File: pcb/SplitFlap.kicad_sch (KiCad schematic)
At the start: 22 parts, among them J1 A1_3, U1 PCF8575DBR, U2 ULN2003, U4 AP2112K-3.3

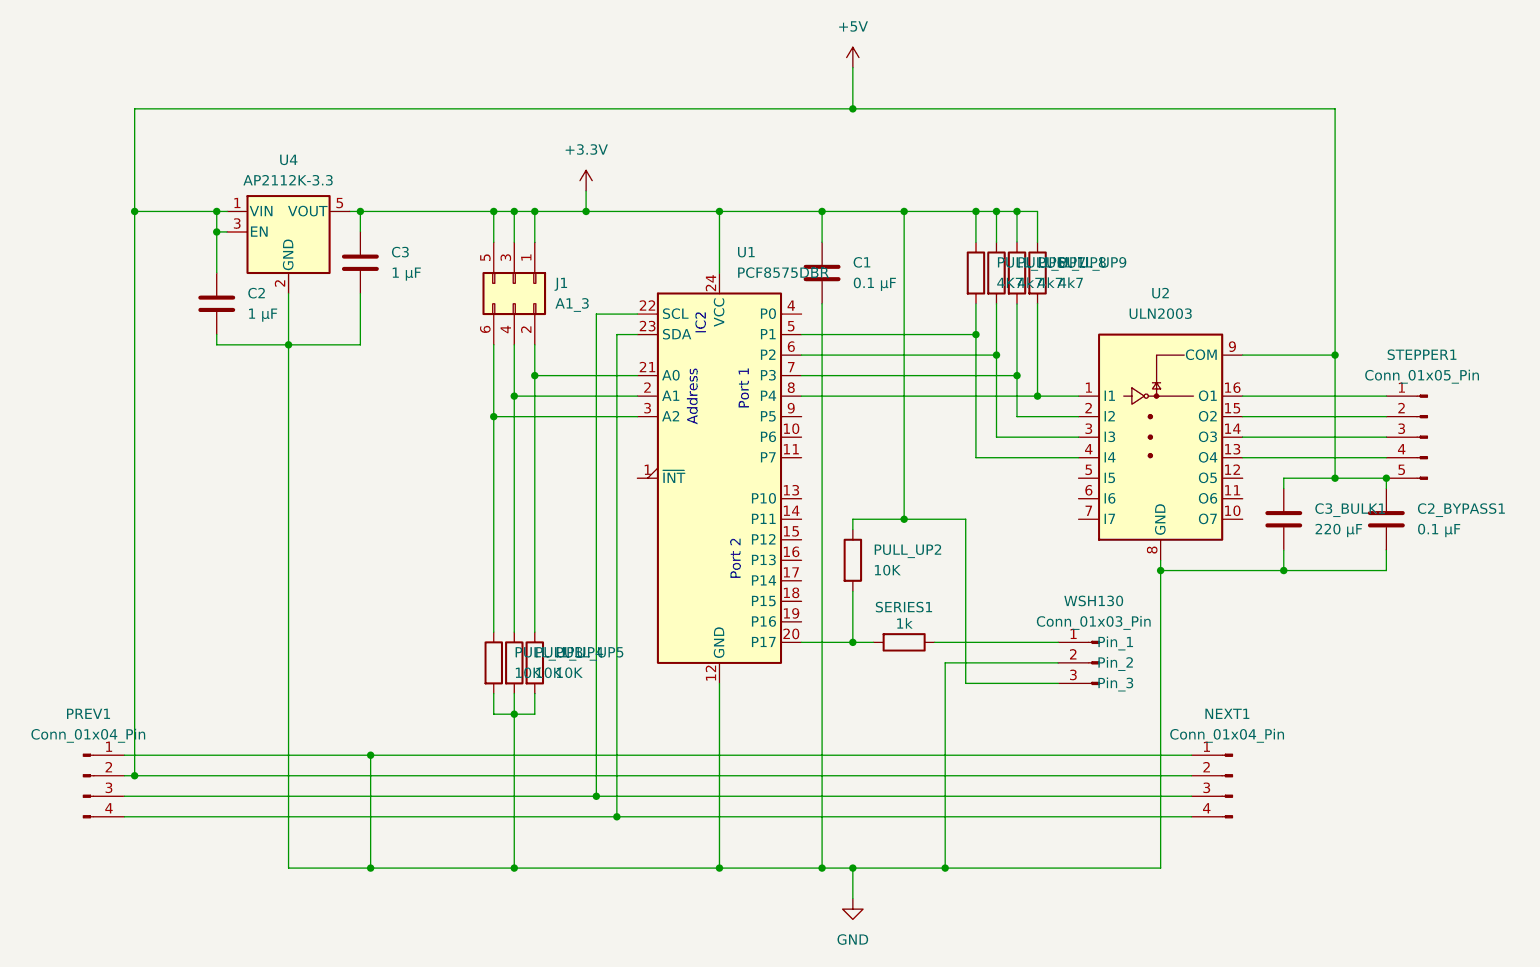
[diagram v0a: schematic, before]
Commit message: Eliminate 3.3v line from PCB
Based on the findings by FoxManJ the 3.3v line is not required if we
use a 4.7k Ohm pull-up to 5v for the SCL and SDA lines coming from the
ESP32.

By using this pull-up to 5V we eliminate the need for the PCF8575 to
run at 3.3v to understand the signals from the ESP32, which was the
reason I originally implemented the 3.3v line on each board.
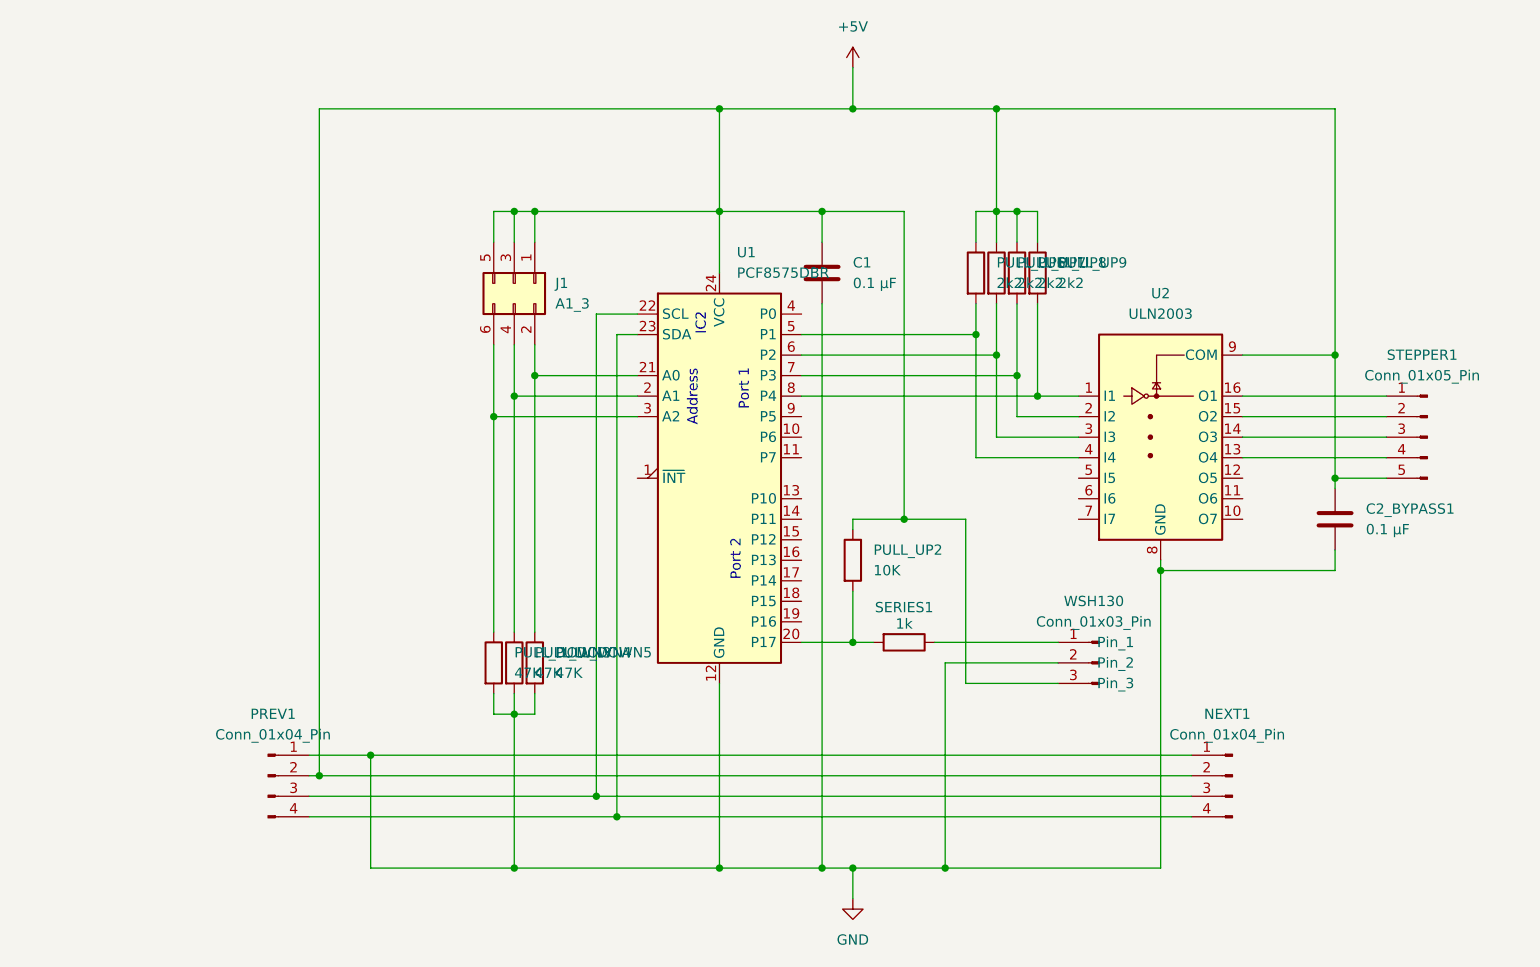
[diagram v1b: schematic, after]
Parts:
- removed C2, C3: 1 µF, Capacitor_SMD:C_0603_1608Metric, symbol Device:C
- removed C3_BULK1: 220 µF, Capacitor_SMD:C_Elec_6.3x7.7, symbol Device:C
- removed U4: AP2112K-3.3, Package_TO_SOT_SMD:SOT-23-5, symbol Regulator_Linear:AP2112K-3.3
- PULL_DOWN3: renamed from PULL_UP3; value 10K -> 47K
- PULL_DOWN4: renamed from PULL_UP4; value 10K -> 47K
- PULL_DOWN5: renamed from PULL_UP5; value 10K -> 47K
- PULL_UP6: value 4K7 -> 2k2
- PULL_UP7, PULL_UP8, PULL_UP9: value 4k7 -> 2k2
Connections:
- net +3.3V is gone; now on net +5V: C1.1, J1.1 (Pin_1), J1.3 (Pin_3), J1.5 (Pin_5), PULL_UP2.1, PULL_UP6.1, PULL_UP7.1, PULL_UP8.1, PULL_UP9.1, U1.24 (VCC), WSH130.3 (Pin_3)
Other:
- moved on the sheet: C2_BYPASS1, PREV1

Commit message: Use pinsocket and headers for board to board connector
Eliminates the JST cables between boards.
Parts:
- J1: MPN (none) -> C7501594
- NEXT1: footprint Connector_JST:JST_PH_B4B-PH-K_1x04_P2.00mm_Vertical -> Connector_PinSocket_2.54mm:PinSocket_1x04_P2.54mm_Horizontal; MPN C2321 -> C6297769
- PREV1: footprint Connector_JST:JST_PH_B4B-PH-K_1x04_P2.00mm_Vertical -> Connector_PinHeader_2.54mm:PinHeader_1x04_P2.54mm_Horizontal; MPN C2321 -> C22438278
- PULL_DOWN3, PULL_DOWN4, PULL_DOWN5: MPN C73809 -> C25600
- PULL_UP6, PULL_UP7, PULL_UP8, PULL_UP9: MPN C23162 -> C4190
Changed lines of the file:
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@@
 			)
 		)
-		(property "MPN" "C23162"
+		(property "MPN" "C4190"
 			(at 165.1 68.58 0)
 			(effects
@@
 			)
 		)
-		(property "MPN" "C73809"
+		(property "MPN" "C25600"
 			(at 97.79 116.84 0)
 			(effects
@@
 			)
 		)
-		(property "MPN" "C73809"
+		(property "MPN" "C25600"
 			(at 100.33 116.84 0)
 			(effects
@@
 			)
 		)
-		(property "MPN" "C23162"
+		(property "MPN" "C4190"
 			(at 160.02 68.58 0)
 			(effects
@@
 			)
 		)
-		(property "Footprint" "Connector_JST:JST_PH_B4B-PH-K_1x04_P2.00mm_Vertical"
+		(property "Footprint" "Connector_PinSocket_2.54mm:PinSocket_1x04_P2.54mm_Horizontal"
 			(at 189.23 130.81 0)
 			(effects
@@
 			)
 		)
-		(property "MPN" "C2321"
+		(property "MPN" "C6297769"
 			(at 189.23 130.81 0)
 			(effects
@@
 			)
 		)
-		(property "MPN" "C23162"
+		(property "MPN" "C4190"
 			(at 157.48 68.58 0)
 			(effects
@@
 			)
 		)
-		(property "MPN" "C73809"
+		(property "MPN" "C25600"
 			(at 102.87 116.84 0)
 			(effects
@@
 			)
 		)
+		(property "MPN" "C7501594"
+			(at 100.33 69.85 90)
+			(effects
+				(font
+					(size 1.27 1.27)
+				)
+				(hide yes)
+			)
+		)
 		(pin "1"
 		)
@@
 			)
 		)
-		(property "Footprint" "Connector_JST:JST_PH_B4B-PH-K_1x04_P2.00mm_Vertical"
+		(property "Footprint" "Connector_PinHeader_2.54mm:PinHeader_1x04_P2.54mm_Horizontal"
 			(at 69.85 130.81 0)
 			(effects
@@
 			)
 		)
-		(property "MPN" "C2321"
+		(property "MPN" "C22438278"
 			(at 69.85 130.81 0)
 			(effects
@@
 			)
 		)
-		(property "MPN" "C23162"
+		(property "MPN" "C4190"
 			(at 162.56 68.58 0)
 			(effects

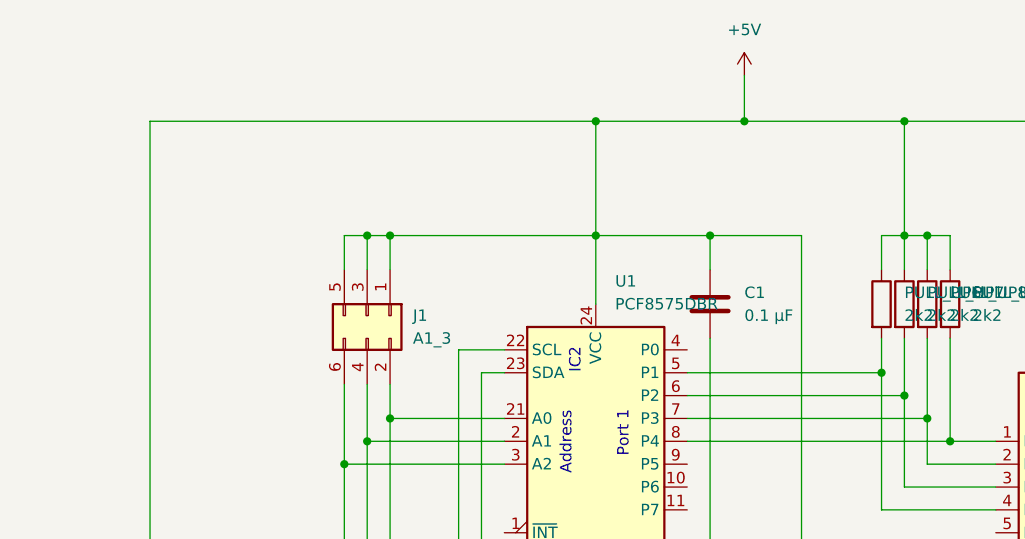
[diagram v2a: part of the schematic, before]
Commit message: Add optional data lines pull-up
Required as the ESP32 by default does not pull up the data lines to
5v.  Should only be activated once per circuit (display).
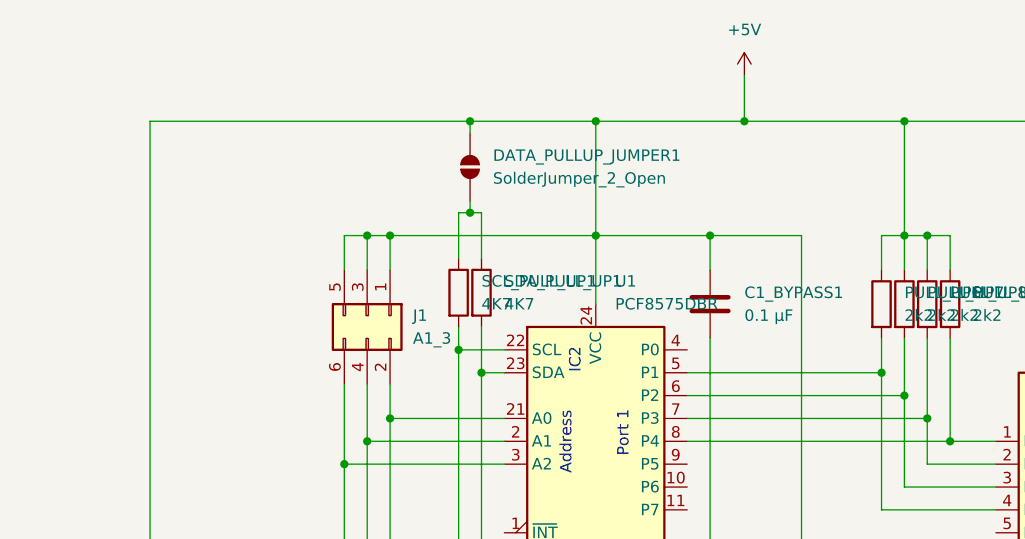
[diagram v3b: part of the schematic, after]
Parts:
- added DATA_PULLUP_JUMPER1: SolderJumper_2_Open, Jumper:SolderJumper-2_P1.3mm_Open_RoundedPad1.0x1.5mm, symbol Jumper:SolderJumper_2_Open
- added SCL_PULL_UP1, SDA_PULL_UP1: 4K7, Resistor_SMD:R_0603_1608Metric, symbol Device:R
- C1_BYPASS1: renamed from C1; MPN C6955083 -> C1525
- C2_BYPASS1: MPN C6955083 -> C1525
- NEXT1: MPN C6297769 -> C2897386
- PREV1: MPN C22438278 -> C91552
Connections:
- net +5V: now also DATA_PULLUP_JUMPER1.1 (A)
- net at NEXT1.3 (Pin_3), PREV1.3 (Pin_3), U1.22 (SCL): now also SCL_PULL_UP1.2
- net at NEXT1.4 (Pin_4), PREV1.4 (Pin_4), U1.23 (SDA): now also SDA_PULL_UP1.2
- new net: DATA_PULLUP_JUMPER1.2 (B), SCL_PULL_UP1.1, SDA_PULL_UP1.1

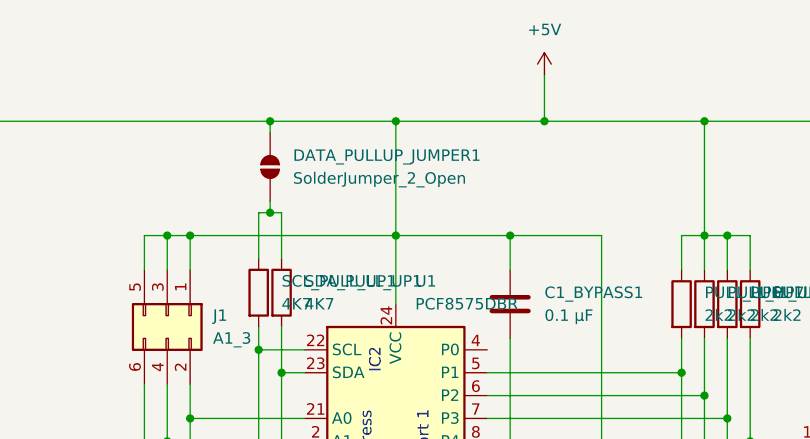
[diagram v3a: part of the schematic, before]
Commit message: Rename pull-up jumper
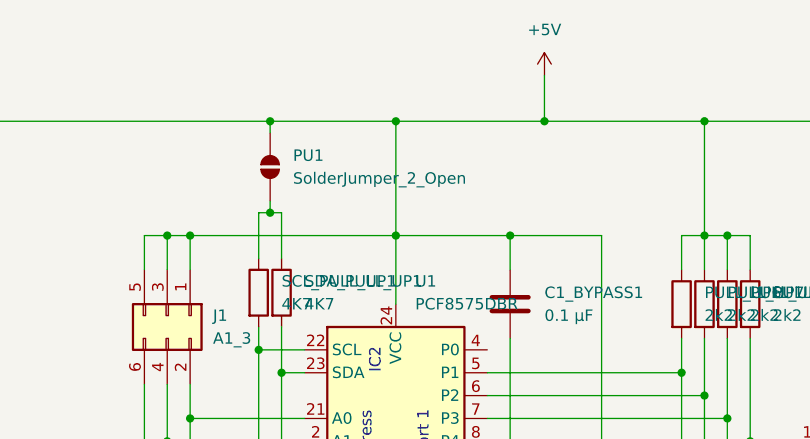
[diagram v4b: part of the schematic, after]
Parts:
- renumbered DATA_PULLUP_JUMPER1 to PU1
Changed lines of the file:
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@@
 		(dnp no)
 		(fields_autoplaced yes)
-		(property "Reference" "DATA_PULLUP_JUMPER1"
+		(property "Reference" "PU1"
 			(at 114.3 52.0699 90)
 			(effects
@@
 			(project ""
 				(path "/a27c2069-9cb4-4119-a6b4-dc99fc554c69"
-					(reference "DATA_PULLUP_JUMPER1")
+					(reference "PU1")
 					(unit 1)
 				)

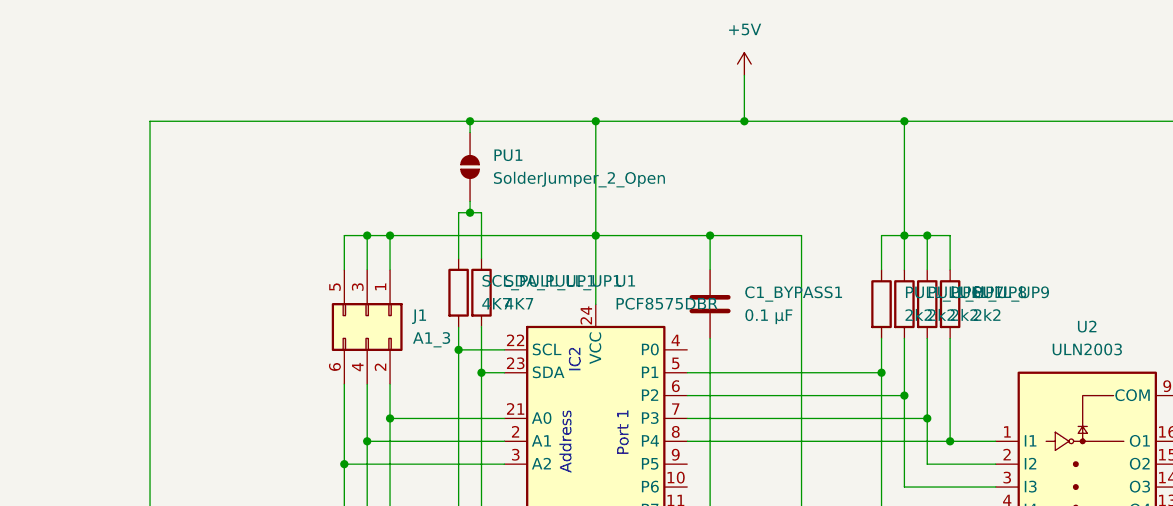
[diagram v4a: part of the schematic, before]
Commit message: Fix floating pull-ups
The optional pull-ups added in v4 added an unintentional floating node
that would tie SCL and SDA together whenever the pull-up pad was
unsoldered.  Causing the I2C bus to fail (surprisingly only after
connecting 3 modules).
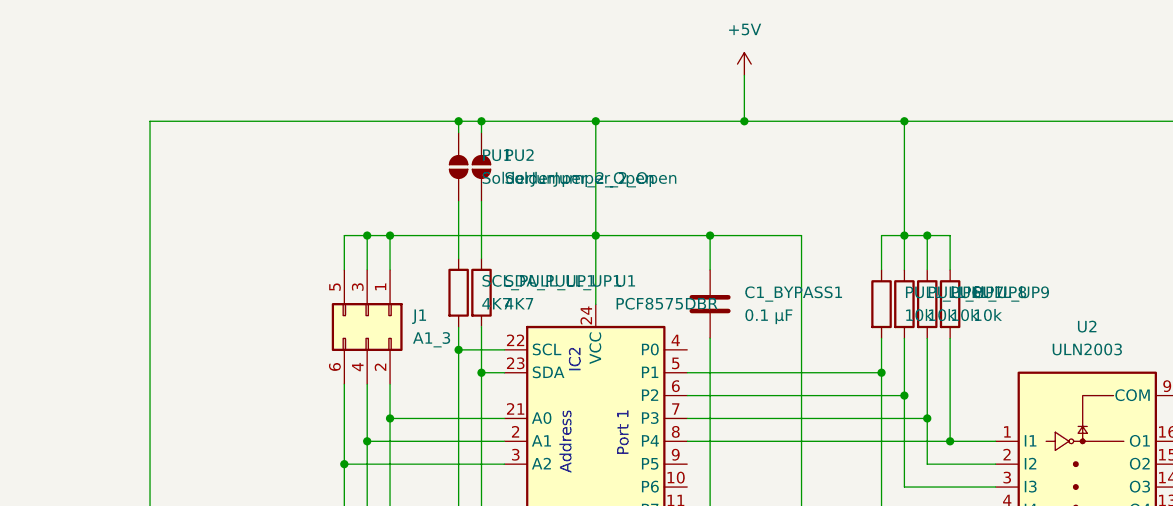
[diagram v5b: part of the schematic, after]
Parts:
- added PU2: SolderJumper_2_Open, Jumper:SolderJumper-2_P1.3mm_Open_RoundedPad1.0x1.5mm, symbol Jumper:SolderJumper_2_Open
- PULL_UP6, PULL_UP7, PULL_UP8, PULL_UP9: value 2k2 -> 10k; MPN C4190 -> C73809
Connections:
- net +5V: now also PU2.1 (A)
- net at PU1.2 (B), SCL_PULL_UP1.1: no longer SDA_PULL_UP1.1
- new net: PU2.2 (B), SDA_PULL_UP1.1
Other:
- moved on the sheet: PU1
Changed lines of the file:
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@@
+	)
+	(junction
+		(at 113.03 48.26)
+		(diameter 0)
+		(color 0 0 0 0)
 	)
 	(junction
@@
 	)
 	(junction
-		(at 111.76 48.26)
-		(diameter 0)
-		(color 0 0 0 0)
-	)
-	(junction
 		(at 160.02 60.96)
 		(diameter 0)
@@
 	)
 	(junction
+		(at 110.49 48.26)
+		(diameter 0)
+		(color 0 0 0 0)
+	)
+	(junction
 		(at 100.33 83.82)
 		(diameter 0)
@@
 	)
 	(junction
-		(at 111.76 58.42)
-		(diameter 0)
-		(color 0 0 0 0)
-	)
-	(junction
 		(at 138.43 60.96)
 		(diameter 0)
@@
 	(wire
 		(pts
-			(xy 76.2 48.26) (xy 111.76 48.26)
+			(xy 76.2 48.26) (xy 110.49 48.26)
 		)
 		(stroke
@@
 	(wire
 		(pts
-			(xy 111.76 58.42) (xy 113.03 58.42)
-		)
-		(stroke
-			(width 0)
-			(type default)
-		)
-	)
-	(wire
-		(pts
 			(xy 162.56 60.96) (xy 165.1 60.96)
 		)
@@
 	(wire
 		(pts
-			(xy 110.49 63.5) (xy 110.49 58.42)
+			(xy 110.49 57.15) (xy 110.49 63.5)
 		)
 		(stroke
@@
 	(wire
 		(pts
+			(xy 113.03 48.26) (xy 125.73 48.26)
+		)
+		(stroke
+			(width 0)
+			(type default)
+		)
+	)
+	(wire
+		(pts
 			(xy 100.33 60.96) (xy 100.33 64.77)
 		)
@@
 	(wire
 		(pts
-			(xy 111.76 48.26) (xy 125.73 48.26)
-		)
-		(stroke
-			(width 0)
-			(type default)
-		)
-	)
-	(wire
-		(pts
 			(xy 142.24 107.95) (xy 142.24 114.3)
 		)
@@
 	(wire
 		(pts
-			(xy 111.76 57.15) (xy 111.76 58.42)
-		)
-		(stroke
-			(width 0)
-			(type default)
-		)
-	)
-	(wire
-		(pts
 			(xy 160.02 72.39) (xy 160.02 78.74)
 		)
@@
 	(wire
 		(pts
+			(xy 110.49 48.26) (xy 113.03 48.26)
+		)
+		(stroke
+			(width 0)
+			(type default)
+		)
+	)
+	(wire
+		(pts
 			(xy 110.49 133.35) (xy 184.15 133.35)
 		)
@@
 	(wire
 		(pts
-			(xy 113.03 58.42) (xy 113.03 63.5)
+			(xy 113.03 57.15) (xy 113.03 63.5)
 		)
 		(stroke
@@
 	(wire
 		(pts
+			(xy 113.03 48.26) (xy 113.03 49.53)
+		)
+		(stroke
+			(width 0)
+			(type default)
+		)
+	)
+	(wire
+		(pts
 			(xy 113.03 71.12) (xy 113.03 76.2)
 		)
@@
 	(wire
 		(pts
-			(xy 110.49 58.42) (xy 111.76 58.42)
-		)
-		(stroke
-			(width 0)
-			(type default)
-		)
-	)
-	(wire
-		(pts
 			(xy 115.57 83.82) (xy 100.33 83.82)
 		)
@@
 	(wire
 		(pts
-			(xy 111.76 48.26) (xy 111.76 49.53)
+			(xy 110.49 48.26) (xy 110.49 49.53)
 		)
 		(stroke
@@
 			)
 		)
-		(property "Value" "2k2"
+		(property "Value" "10k"
 			(at 167.64 69.8499 0)
 			(effects
@@
 			)
 		)
-		(property "MPN" "C4190"
+		(property "MPN" "C73809"
 			(at 165.1 68.58 0)
 			(effects
@@
 	(symbol
 		(lib_id "Jumper:SolderJumper_2_Open")
-		(at 111.76 53.34 270)
+		(at 110.49 53.34 270)
 		(unit 1)
 		(exclude_from_sim no)
@@
 		(fields_autoplaced yes)
 		(property "Reference" "PU1"
-			(at 114.3 52.0699 90)
+			(at 113.03 52.0699 90)
 			(effects
 				(font
@@
 		)
 		(property "Value" "SolderJumper_2_Open"
-			(at 114.3 54.6099 90)
+			(at 113.03 54.6099 90)
 			(effects
 				(font
@@
 		)
 		(property "Footprint" "Jumper:SolderJumper-2_P1.3mm_Open_RoundedPad1.0x1.5mm"
-			(at 111.76 53.34 0)
+			(at 110.49 53.34 0)
 			(effects
 				(font
@@
 		)
 		(property "Datasheet" "~"
-			(at 111.76 53.34 0)
+			(at 110.49 53.34 0)
 			(effects
 				(font
@@
 		)
 		(property "Description" "Solder Jumper, 2-pole, open"
-			(at 111.76 53.34 0)
+			(at 110.49 53.34 0)
 			(effects
 				(font
@@
 			)
 		)
-		(property "Value" "2k2"
+		(property "Value" "10k"
 			(at 162.56 69.8499 0)
 			(effects
@@
 			)
 		)
-		(property "MPN" "C4190"
+		(property "MPN" "C73809"
 			(at 160.02 68.58 0)
 			(effects
@@
 			)
 		)
-		(property "Value" "2k2"
+		(property "Value" "10k"
 			(at 160.02 69.8499 0)
 			(effects
@@
 			)
 		)
-		(property "MPN" "C4190"
+		(property "MPN" "C73809"
 			(at 157.48 68.58 0)
 			(effects
@@
 	)
 	(symbol
+		(lib_id "Jumper:SolderJumper_2_Open")
+		(at 113.03 53.34 270)
+		(unit 1)
+		(exclude_from_sim no)
+		(in_bom no)
+		(on_board yes)
+		(dnp no)
+		(fields_autoplaced yes)
+		(property "Reference" "PU2"
+			(at 115.57 52.0699 90)
+			(effects
+				(font
+					(size 1.27 1.27)
+				)
+				(justify left)
+			)
+		)
+		(property "Value" "SolderJumper_2_Open"
+			(at 115.57 54.6099 90)
+			(effects
+				(font
+					(size 1.27 1.27)
+				)
+				(justify left)
+			)
+		)
+		(property "Footprint" "Jumper:SolderJumper-2_P1.3mm_Open_RoundedPad1.0x1.5mm"
+			(at 113.03 53.34 0)
+			(effects
+				(font
+					(size 1.27 1.27)
+				)
+				(hide yes)
+			)
+		)
+		(property "Datasheet" "~"
+			(at 113.03 53.34 0)
+			(effects
+				(font
+					(size 1.27 1.27)
+				)
+				(hide yes)
+			)
+		)
+		(property "Description" "Solder Jumper, 2-pole, open"
+			(at 113.03 53.34 0)
+			(effects
+				(font
+					(size 1.27 1.27)
+				)
+				(hide yes)
+			)
+		)
+		(pin "2"
+		)
+		(pin "1"
+		)
+		(instances
+			(project "SplitFlap"
+				(path "/a27c2069-9cb4-4119-a6b4-dc99fc554c69"
+					(reference "PU2")
+					(unit 1)
+				)
+			)
+		)
+	)
+	(symbol
 		(lib_id "Device:R")
 		(at 102.87 116.84 0)
@@
 			)
 		)
-		(property "Value" "2k2"
+		(property "Value" "10k"
 			(at 165.1 69.8499 0)
 			(effects
@@
 			)
 		)
-		(property "MPN" "C4190"
+		(property "MPN" "C73809"
 			(at 162.56 68.58 0)
 			(effects
